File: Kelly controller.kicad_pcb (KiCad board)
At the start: 2 copper layers, 65.4 x 54.3 mm, 16 parts, among them J2 Conn_01x12_Female, J3 Batt, J4 Meter, J5 48V, J6 12V, J7 5V, SW1 FNR, SW2 Foot Switch, SW3 Brake, SW4 Power Switch

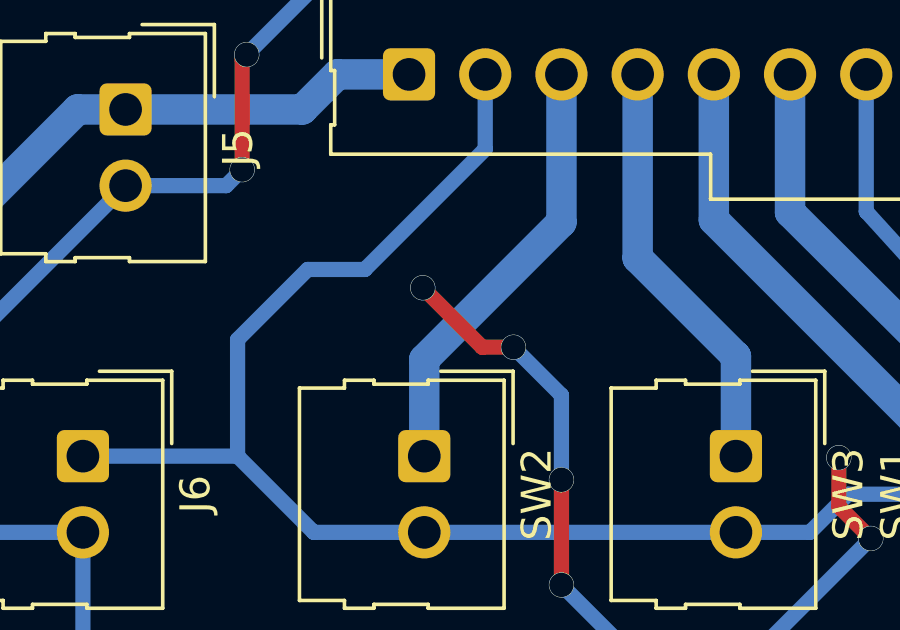
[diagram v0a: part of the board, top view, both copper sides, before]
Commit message: trying to fix via sizes
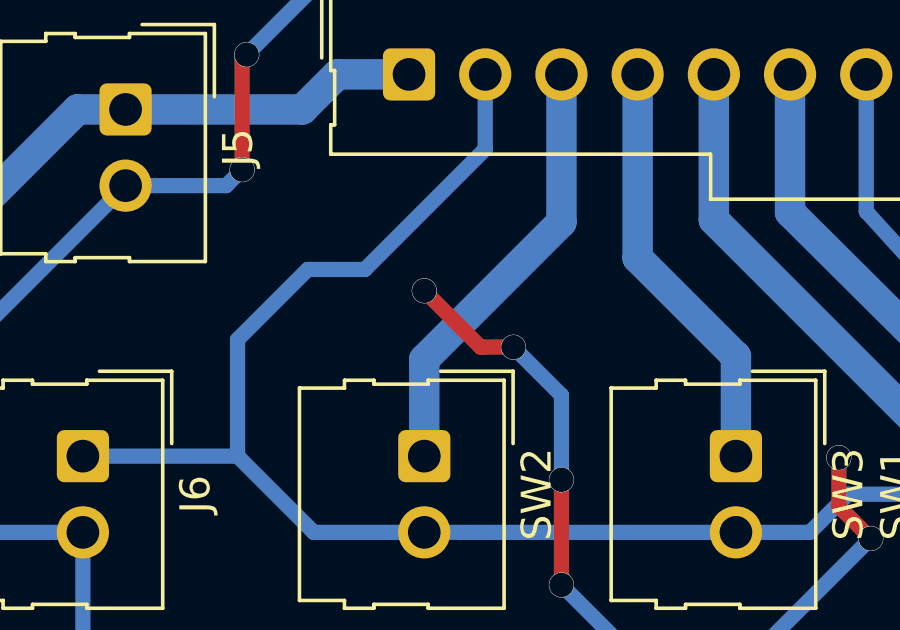
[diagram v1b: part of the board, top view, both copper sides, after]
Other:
- net class Default: via_dia 0.8128 -> 0.8382; via_drill 0.4064 -> 0.8128
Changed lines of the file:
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@@
     (thickness 1.6)
     (drawings 4)
-    (tracks 150)
+    (tracks 151)
     (zones 0)
     (modules 16)
@@
     (zone_45_only no)
     (trace_min 0.254)
-    (via_size 0.8128)
-    (via_drill 0.4064)
+    (via_size 0.8382)
+    (via_drill 0.8128)
     (via_min_size 0.4064)
     (via_min_drill 0.4064)
     (user_via 0.8382 0.8128)
+    (user_via 0.889 0.8128)
     (uvia_size 0.8128)
     (uvia_drill 0.4064)
@@
     (clearance 0.254)
     (trace_width 0.254)
-    (via_dia 0.8128)
-    (via_drill 0.4064)
+    (via_dia 0.8382)
+    (via_drill 0.8128)
     (uvia_dia 0.8128)
     (uvia_drill 0.4064)
@@
   (segment (start 128.4732 69.1896) (end 128.4732 66.3702) (width 0.508) (layer B.Cu) (net 12))
   (segment (start 128.4732 66.3702) (end 126.873 64.77) (width 0.508) (layer B.Cu) (net 12))
-  (via (at 123.8504 62.7888) (size 0.8382) (drill 0.8128) (layers F.Cu B.Cu) (net 12))
   (segment (start 126.873 64.77) (end 125.8316 64.77) (width 0.508) (layer F.Cu) (net 12))
-  (segment (start 125.8316 64.77) (end 123.8504 62.7888) (width 0.508) (layer F.Cu) (net 12))
   (via (at 138.7856 71.1454) (size 0.8382) (drill 0.8128) (layers F.Cu B.Cu) (net 12))
   (segment (start 132.7912 77.0128) (end 132.9182 77.0128) (width 0.508) (layer B.Cu) (net 12))
@@
   (via (at 137.7188 68.453) (size 0.8382) (drill 0.8128) (layers F.Cu B.Cu) (net 12))
   (segment (start 137.7188 70.0786) (end 137.7188 68.453) (width 0.508) (layer F.Cu) (net 12))
+  (segment (start 125.8316 64.77) (end 125.7808 64.77) (width 0.508) (layer F.Cu) (net 12))
+  (via (at 123.9012 62.8904) (size 0.8382) (drill 0.8128) (layers F.Cu B.Cu) (net 12))
+  (segment (start 125.7808 64.77) (end 123.9012 62.8904) (width 0.508) (layer F.Cu) (net 12))
   (zone (net 12) (net_name GND) (layer B.Cu) (hatch edge 0.508)
     (connect_pads (clearance 0.508))

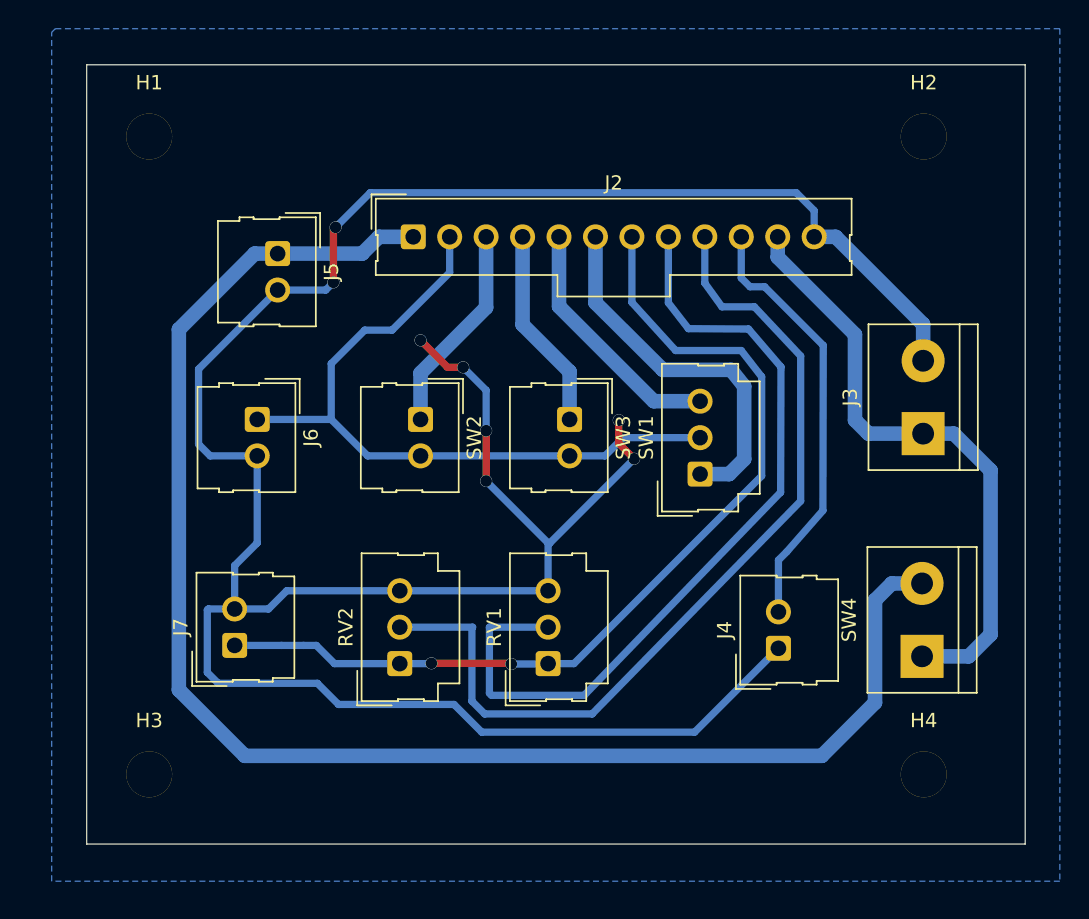
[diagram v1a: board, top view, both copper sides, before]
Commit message: Split 12 pin connector realized did not have 12 pin connector so split roughly into power and controls cables redid pcb layout and exported gerbers;
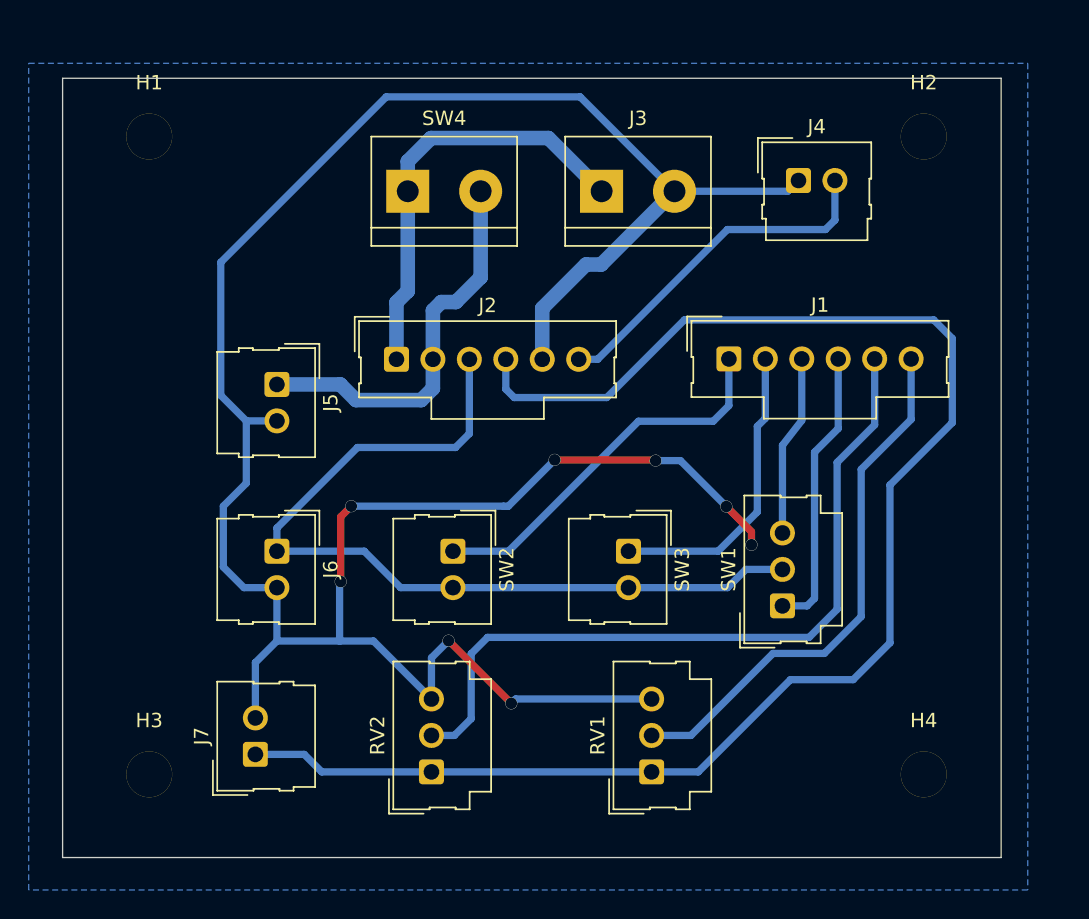
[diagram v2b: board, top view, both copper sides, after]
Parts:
- added J1: Conn_01x06_Female, Connector_Molex:Molex_SL_171971-0006_1x06_P2.54mm_Vertical, F.Cu at (145.4, 64.2)
- J2: value Conn_01x12_Female -> Conn_01x06_Female; footprint Connector_Molex:Molex_SL_171971-0012_1x12_P2.54mm_Vertical -> Connector_Molex:Molex_SL_171971-0006_1x06_P2.54mm_Vertical
- moved SW4 48.3 mm to (123.0, 52.5), turned to 0 degrees
- moved J4 32.6 mm to (150.2, 51.8), turned to 0 degrees
- moved J3 28.1 mm to (136.5, 52.5), turned to 0 degrees
- moved SW1 10.8 mm to (149.1, 81.4)
- moved RV1 10.4 mm to (140.0, 93.0)
- moved SW3 10.1 mm to (138.4, 77.6)
- moved SW2 9.46 mm to (126.2, 77.6)
- moved J6 9.28 mm to (113.9, 77.6)
- moved J5 9.12 mm to (113.9, 66.0)
- moved J2 8.61 mm to (122.2, 64.2)
- moved RV2 7.86 mm to (124.7, 93.0)
- moved J7 7.73 mm to (112.4, 91.7)
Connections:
- J2 pad 1: +48V -> /PWR
- J2 pad 2: 12V -> +48V
- J2 pad 3: /Foot_SW -> 12V
- J2 pad 4: /Brake -> 5V
- J2 pad 5: /REV -> GND
- J2 pad 6: /FWD -> /Meter
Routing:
- net +48V: track 107.0 -> 27.4 mm
- net 5V: track 65.6 -> 107.7 mm, vias 2 -> 0
- net /Throttle: track 58.3 -> 37.4 mm
- net GND: track 192.1 -> 178.1 mm
- net /PWR: track 42.7 -> 29.8 mm
- net /Foot_SW: track 14.6 -> 26.7 mm
- net 12V: track 49.7 -> 59.7 mm
- net /Brake_AN: track 62.1 -> 53.1 mm
- net /Brake: track 14.1 -> 21.0 mm
- net /FWD: track 26.0 -> 19.8 mm
- net /Meter: track 30.3 -> 24.6 mm
- net /REV: track 17.4 -> 12.6 mm

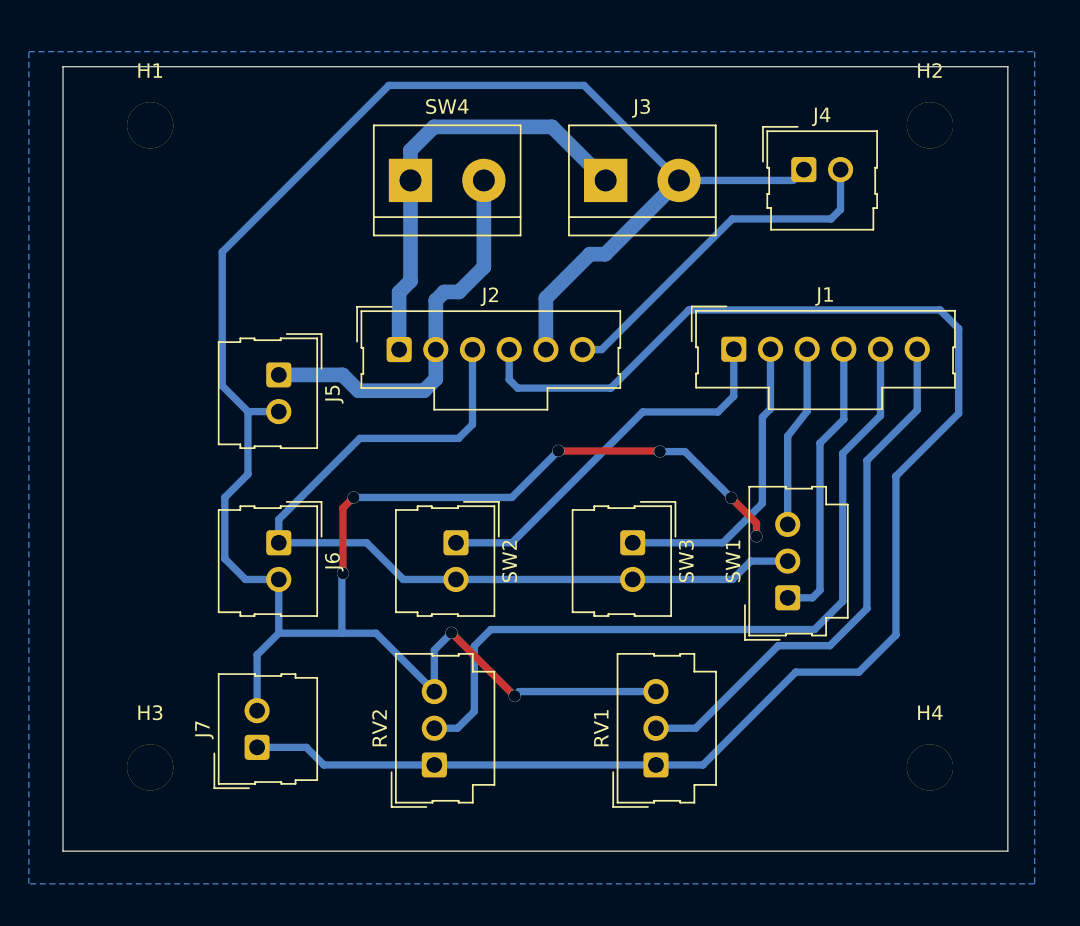
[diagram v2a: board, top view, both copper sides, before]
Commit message: Ready to cut second board
Thickened 12V traces and removed batt connector which was superfluous
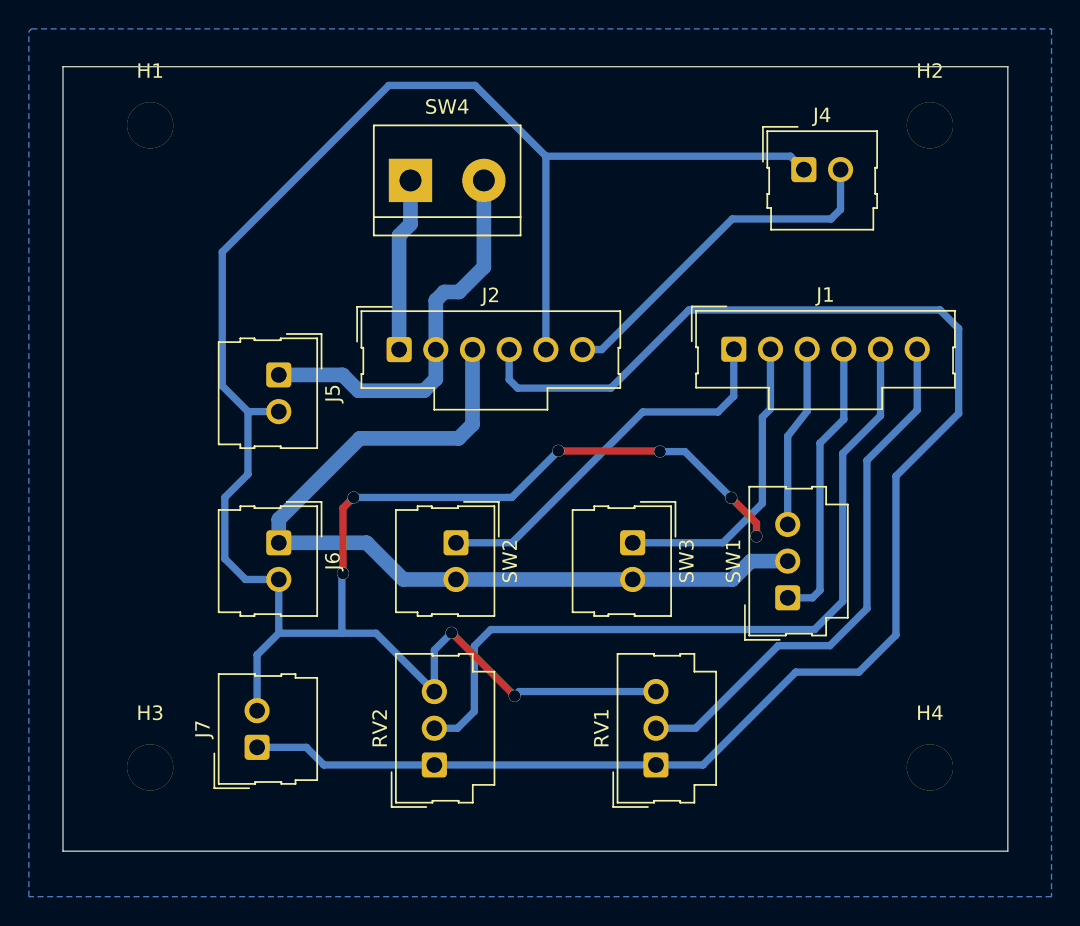
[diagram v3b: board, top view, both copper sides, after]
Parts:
- removed J3: Batt, TerminalBlock:TerminalBlock_bornier-2_P5.08mm
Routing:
- net /PWR: track 29.8 -> 12.0 mm
- net GND: track 178.1 -> 174.7 mm

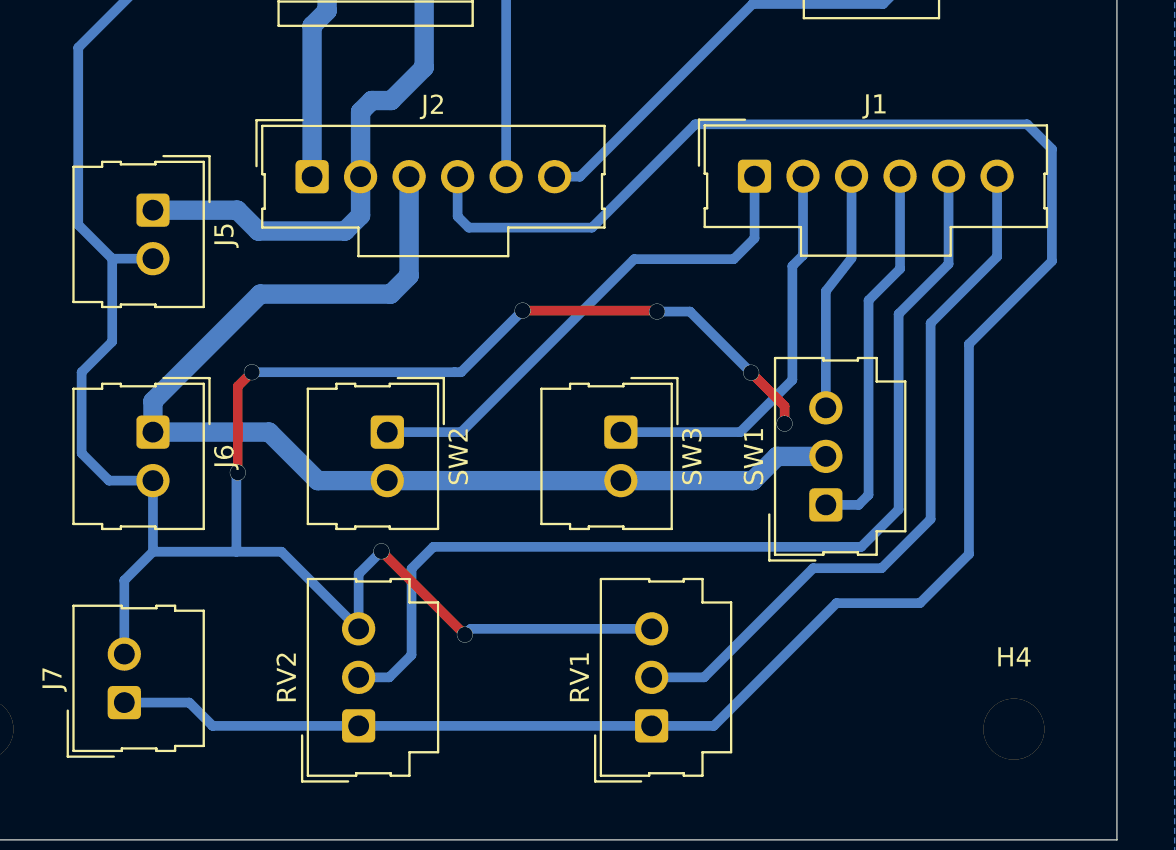
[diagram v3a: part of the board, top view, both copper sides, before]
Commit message: minor routing changes to improve cutting time
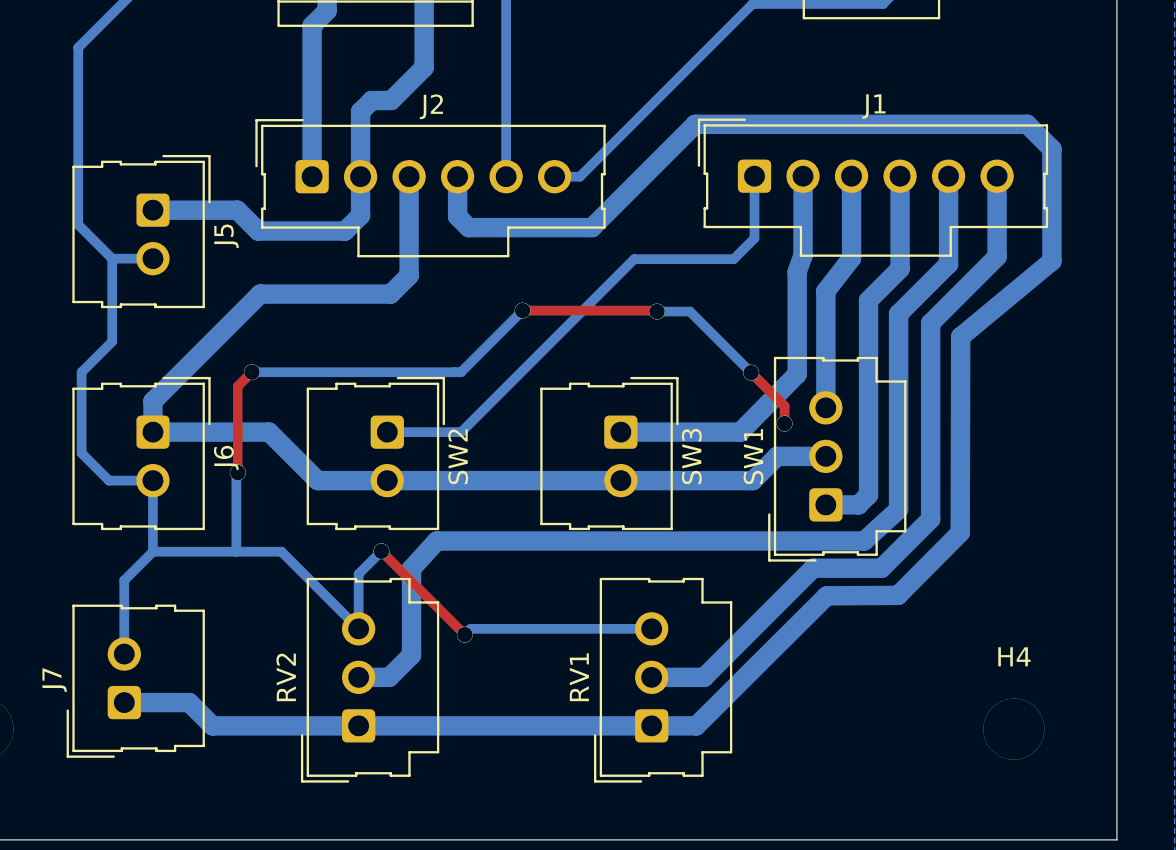
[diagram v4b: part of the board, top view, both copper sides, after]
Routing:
- net 5V: track 107.7 -> 107.0 mm
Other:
- rule via_min_drill: 0.4064 -> 0.8128
- rule via_min_size: 0.4064 -> 0.8382
